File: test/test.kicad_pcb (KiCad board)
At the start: 2 copper layers, 100 x 100 mm, 107 parts, among them J1 UEXT_Host, J2 Conn_01x02, J3 Conn_02x06_Odd_Even, J4 Conn_02x06_Odd_Even, J5 Conn_02x06_Odd_Even, Q1 BC859, Q10 BC848, Q11 BC808, Q12 BC848, Q13 BC848, Q14 BC808, Q15 BC848, Q16 BC808, Q17 BC808, Q2 BC859, Q3 BC859, Q4 BC859, Q5 BC859, Q6 BC848, Q7 BC808, Q8 BC848, Q9 BC808, U3 PCA9531PW, U4 PCF8574AT, U6 TLC59108FPW

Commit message: work on 2nd update test
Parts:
- removed C1, C5, C6: C, PCM_Diode_SMD_Handsoldering_AKL:D_0603_1608Metric
- removed C2, C3, C4: C_Polarized, Capacitor_THT:CP_Radial_D5.0mm_P2.00mm
- removed D10, D11, D12, D13, D14, D15, D6, D7, D8, D9: LED, LED_THT:LED_D3.0mm
- removed J3, J4, J5: Conn_02x06_Odd_Even, Connector_PinHeader_2.54mm:PinHeader_2x06_P2.54mm_Vertical
- removed Q1, Q2, Q3, Q4, Q5: BC859, Package_TO_SOT_SMD:SOT-23
- removed Q10, Q12, Q13, Q15, Q6, Q8: BC848, Package_TO_SOT_SMD:SOT-23
- removed Q11, Q14, Q16, Q17, Q7, Q9: BC808, Package_TO_SOT_SMD:SOT-23
- removed R1, R10, R11, R12, R13, R14, R15, R16, R17, R18, R19, R2, R20, R3, R4, R5, R6, R7, R8, R9: R, Resistor_THT:R_Axial_DIN0204_L3.6mm_D1.6mm_P2.54mm_Vertical
- removed R21, R22, R23, R24, R25, R26, R27, R28, R29, R30, R31, R32, R33, R34, R35, R36, R37, R38, R39, R40, R41, R42, R43, R44, R45, R47, R48, R50, R51, R52, R53: 100k, Resistor_THT:R_Axial_DIN0204_L3.6mm_D1.6mm_P2.54mm_Vertical
- removed R46, R49: 1k, Resistor_THT:R_Axial_DIN0204_L3.6mm_D1.6mm_P2.54mm_Vertical
- removed U1: ~, petkn:THB Miniature Thumbstick THB001P
- added C10: 100n, Capacitor_SMD:C_0805_2012Metric_Pad1.18x1.45mm_HandSolder, B.Cu at (62.9, 127.3)
- added C11: 100n, Capacitor_SMD:C_0805_2012Metric_Pad1.18x1.45mm_HandSolder, B.Cu at (51.5, 127.2)
- added C12: 100n, Capacitor_SMD:C_0805_2012Metric_Pad1.18x1.45mm_HandSolder, B.Cu at (40.8, 126.8)
- added C13: 100n, Capacitor_SMD:C_0805_2012Metric_Pad1.18x1.45mm_HandSolder, B.Cu at (106.3, 124.4)
- added C14: 100n, Capacitor_SMD:C_0805_2012Metric_Pad1.18x1.45mm_HandSolder, B.Cu at (72.4, 135.0)
- added C15: 100u, Capacitor_SMD:C_1206_3216Metric_Pad1.33x1.80mm_HandSolder, B.Cu at (91.6, 134.7)
- added C16: 100u, Capacitor_SMD:C_1206_3216Metric_Pad1.33x1.80mm_HandSolder, B.Cu at (33.6, 134.1)
- added C17: 100n, Capacitor_SMD:C_0805_2012Metric_Pad1.18x1.45mm_HandSolder, B.Cu at (53.4, 134.9)
- added C18: 100u, Capacitor_SMD:C_1206_3216Metric_Pad1.33x1.80mm_HandSolder, B.Cu at (33.6, 105.5)
- added C7: 100n, Capacitor_SMD:C_0805_2012Metric_Pad1.18x1.45mm_HandSolder, B.Cu at (93.5, 124.4)
- added C8: 100n, Capacitor_SMD:C_0805_2012Metric_Pad1.18x1.45mm_HandSolder, B.Cu at (93.5, 121.4)
- added C9: 100n, Capacitor_SMD:C_0805_2012Metric_Pad1.18x1.45mm_HandSolder, B.Cu at (79.1, 127.5)
- added J6: New_PET_keyboard_connector, petkn:PET_New_Keyboard_Connector, F.Cu at (25.1, 100.8)
- added U7: 74LS145, Package_SO:SO-16_3.9x9.9mm_P1.27mm, B.Cu at (79.3, 118.3)
- added U8: ATmega32A-A, Package_QFP:TQFP-44_10x10mm_P0.8mm, B.Cu at (96.9, 102.5)
- added Y1: ASE-xxxMHz, Oscillator:Oscillator_SMD_Abracon_ASE-4Pin_3.2x2.5mm, B.Cu at (106.7, 118.6)
- D1, D2, D3, D4, D5: value LED -> SK6812MINI; footprint LED_THT:LED_D3.0mm -> LED_SMD:LED_SK6812MINI_PLCC4_3.5x3.5mm_P1.75mm; moved to B.Cu
- J1: value UEXT_Host -> AVR-ISP-6; footprint Connector_IDC:IDC-Header_2x05_P2.54mm_Vertical -> Connector_IDC:IDC-Header_2x03_P2.54mm_Vertical
- J2: value Conn_01x02 -> AVR-ISP-6; footprint Connector_PinHeader_2.54mm:PinHeader_1x02_P2.54mm_Vertical -> Connector_IDC:IDC-Header_2x03_P2.54mm_Vertical
- SW1: footprint petkn:SW_Cherry_MX_1.00u_PCB_with_LED -> CherryMX_PCB_LTST-A683CEGBW-Rotated:CherryMX_1.00u_PCB_LTST-A683CEGBW-Rotated
- SW2: value ~ -> CherryMX_LTST-A683CEGBW; footprint petkn:SW_Cherry_MX_1.00u_PCB_with_LED -> petkn:SW_Cherry_MX_1.00u_PCB_with_RGB_LED
- SW3, SW4, SW5: footprint petkn:SW_Cherry_MX_1.00u_PCB_with_LED -> petkn:SW_Cherry_MX_1.00u_PCB_with_RGB_LED
- U2: value ~ -> ATmega32A-A; footprint petkn:true-components-98002c3-ps2-ps3 -> Package_QFP:TQFP-44_10x10mm_P0.8mm; moved to B.Cu
- U3: value PCA9531PW -> 74HCT85; footprint Package_SO:TSSOP-16_4.4x5mm_P0.65mm -> Package_SO:SO-16_3.9x9.9mm_P1.27mm; moved to B.Cu
- U4: value PCF8574AT -> 74LS174; footprint Package_SO:SOIC-16W_7.5x10.3mm_P1.27mm -> Package_SO:SO-16_3.9x9.9mm_P1.27mm; moved to B.Cu
- U6: value TLC59108FPW -> 74LS174; footprint Package_SO:TSSOP-20_4.4x6.5mm_P0.65mm -> Package_SO:SO-16_3.9x9.9mm_P1.27mm; moved to B.Cu
- moved D2 79.1 mm to (24.7, 134.4)
- moved D1 74.4 mm to (44.1, 134.6)
- moved J2 71.1 mm to (95.2, 88.9)
- moved D3 58.0 mm to (63.5, 134.7)
- moved D5 54.2 mm to (101.7, 134.8)
- moved D4 52.8 mm to (82.7, 135.0)
- moved U6 51.6 mm to (40.6, 117.7)
- moved U3 46.9 mm to (63.2, 118.0)
- moved U4 29.9 mm to (51.4, 117.8)
- moved SW3 27.0 mm to (22.9, 153.3)
- moved J1 26.5 mm to (44.1, 87.7), turned to 90 degrees
- moved U5 19.2 mm to (72.1, 96.8)
- moved SW2 19.0 mm to (42.0, 153.3)
- moved U2 9.94 mm to (47.9, 101.4), turned to -90 degrees
- moved SW1 5.69 mm to (101.7, 148.2)
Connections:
- D1 pad 1: Net-(D1-K) -> Net-(D1-DOUT)
- D1 pad 2: Net-(D1-A) -> GND
- D2 pad 1: Net-(D12-K) -> Net-(D1-DIN)
- D2 pad 2: Net-(D2-A) -> GND
- D3 pad 1: Net-(D13-K) -> Net-(D3-DOUT)
- D3 pad 2: Net-(D3-A) -> GND
- D4 pad 1: Net-(D14-K) -> Net-(D4-DOUT)
- D4 pad 2: Net-(D4-A) -> GND
- D5 pad 1: Net-(D10-K) -> unconnected-(D5-DOUT-Pad1)
- D5 pad 2: Net-(D5-A) -> GND
- J1 pad 1: VCC -> Net-(J1-MISO)
- J1 pad 2: GND -> VCC
- J1 pad 3: unconnected-(J1-TXD-Pad3) -> Net-(J1-SCK)
- J1 pad 4: unconnected-(J1-RXD-Pad4) -> Net-(J1-MOSI)
- J1 pad 5: SCL -> Net-(J1-~{RST})
- J1 pad 6: SDA -> GND
- J2 pad 1: VCC5 -> Net-(J2-MISO)
- J2 pad 2: GND -> VCC
- SW1 pad 1: /RES -> Col1
- SW1 pad 2: GND -> Row0
- SW1 pad 3: Net-(D1-K) -> GND
- SW1 pad 4: Net-(R16-Pad1) -> Net-(SW1B-DIN)
- SW2 pad 3: Net-(D12-K) -> GND
- SW2 pad 4: Net-(R17-Pad1) -> Net-(SW1B-DOUT)
- SW3 pad 1: unconnected-(SW3-Pad1) -> Col5
- SW3 pad 2: unconnected-(SW3-Pad2) -> Row0
- SW3 pad 3: Net-(D13-K) -> GND
- SW4 pad 1: unconnected-(SW4-Pad1) -> Col5
- SW4 pad 2: unconnected-(SW4-Pad2) -> Row8
- SW4 pad 3: Net-(D14-K) -> GND
- SW4 pad 4: Net-(R19-Pad1) -> Net-(SW3B-DOUT)
- SW5 pad 1: unconnected-(SW5-Pad1) -> Col1
- SW5 pad 2: unconnected-(SW5-Pad2) -> Row8
- SW5 pad 3: Net-(D10-K) -> GND
- SW5 pad 4: Net-(R20-Pad1) -> Net-(SW4B-DOUT)
- U2 pad 1: (no net) -> Net-(J1-MOSI)
- U2 pad 10: Net-(J4-Pin_3) -> Net-(U2-PD1)
- U2 pad 11: Net-(J4-Pin_5) -> Net-(U2-PD2)
- U2 pad 12: Net-(J4-Pin_2) -> Net-(U2-PB4)
- U2 pad 13: Net-(J4-Pin_4) -> Col4
- U2 pad 14: Net-(J4-Pin_6) -> Col5
- U2 pad 2: (no net) -> Net-(J1-MISO)
- U2 pad 3: (no net) -> Net-(J1-SCK)
- U2 pad 4: (no net) -> Net-(J1-~{RST})
- U2 pad 5: Net-(J4-Pin_9) -> VCC
- U2 pad 6: Net-(J4-Pin_7) -> GND
- U2 pad 7: Net-(J4-Pin_10) -> unconnected-(U2-XTAL2-Pad7)
- U2 pad 8: Net-(J4-Pin_8) -> CLK16M
- U2 pad 9: Net-(J4-Pin_1) -> Net-(U2-PD0)
- U3 pad 1: GND -> S3
- U3 pad 10: unconnected-(U3-LED5-Pad10) -> Net-(U3-A0)
- U3 pad 11: unconnected-(U3-LED6-Pad11) -> S1
- U3 pad 12: unconnected-(U3-LED7-Pad12) -> Net-(U3-A1)
- U3 pad 13: /RES -> Net-(U3-A2)
- U3 pad 14: SCL -> S2
- U3 pad 15: SDA -> Net-(U3-A3)
- U3 pad 2: GND -> unconnected-(U3-Ia<b-Pad2)
- U3 pad 3: GND -> VCC
- U3 pad 4: PWM0 -> unconnected-(U3-Ia>b-Pad4)
- U3 pad 5: PWM1 -> unconnected-(U3-Oa>b-Pad5)
- U3 pad 6: PWM2 -> Net-(U2-PD2)
- U3 pad 7: PWM3 -> unconnected-(U3-Oa<b-Pad7)
- U3 pad 9: PWM4 -> S0
- U4 pad 1: GND -> VCC
- U4 pad 10: unconnected-(U4-P5-Pad10) -> Net-(U3-A2)
- U4 pad 11: unconnected-(U4-P6-Pad11) -> Net-(U4-D3)
- U4 pad 12: unconnected-(U4-P7-Pad12) -> Net-(U3-A1)
- U4 pad 13: unconnected-(U4-~{INT}-Pad13) -> Net-(U4-D4)
- U4 pad 14: SCL -> Net-(U4-D5)
- U4 pad 15: SDA -> Net-(U3-A0)
- U4 pad 2: GND -> Net-(U4-D3)
- U4 pad 3: GND -> Net-(U4-D0)
- U4 pad 4: ON0 -> Net-(U4-D1)
- U4 pad 5: ON1 -> Net-(U4-D2)
- U4 pad 6: ON2 -> Net-(U4-D2)
- U4 pad 7: ON3 -> Net-(U3-A3)
- U4 pad 9: unconnected-(U4-P4-Pad9) -> CLK16M
- U5 pad 10: Net-(J4-Pin_4) -> Col2
- U5 pad 11: Net-(J4-Pin_6) -> Row5
- U5 pad 12: Net-(J4-Pin_1) -> Row3
- U5 pad 13: Net-(J4-Pin_3) -> Col2
- U5 pad 14: Net-(J4-Pin_3) -> Row4
- U5 pad 5: Net-(J4-Pin_9) -> unconnected-(U5C-SW1_A-Pad5)
- U5 pad 6: Net-(J4-Pin_7) -> unconnected-(U5C-SW1_B-Pad6)
- U5 pad 7: Net-(J4-Pin_10) -> Col4
- U5 pad 8: Net-(J4-Pin_8) -> Row1
- U5 pad 9: Net-(J4-Pin_2) -> Row7
- U6 pad 1: unconnected-(U6-REXT-Pad1) -> VCC
- U6 pad 10: PWM3 -> Net-(U4-D1)
- U6 pad 11: PWM4 -> S3
- U6 pad 12: IO5 -> Net-(U4-D4)
- U6 pad 13: GND -> Net-(U6-D4)
- U6 pad 14: IO6 -> Net-(U6-D5)
- U6 pad 15: IO7 -> Net-(U4-D5)
- U6 pad 16: GND -> VCC
- U6 pad 2: GND -> Net-(U6-D5)
- U6 pad 3: GND -> S0
- U6 pad 4: GND -> S1
- U6 pad 5: GND -> Net-(U6-D4)
- U6 pad 6: PWM0 -> S2
- U6 pad 7: PWM1 -> Net-(U4-D0)
- U6 pad 9: PWM2 -> CLK16M
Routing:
- net VCC: track 262.3 -> 0.00 mm, vias 1 -> 0
- net /RES: track 190.4 -> 0.00 mm, vias 3 -> 0
- net Net-(D12-K): track 134.9 -> 0.00 mm, vias 1 -> 0
- net Net-(D1-K): track 118.3 -> 0.00 mm
- net VCC5: track 116.2 -> 0.00 mm
- net Net-(D14-K): track 104.2 -> 0.00 mm
- net Net-(D13-K): track 100.8 -> 0.00 mm, vias 1 -> 0
- net Net-(Q11-C): track 96.7 -> 0.00 mm
- net Net-(D10-K): track 96.2 -> 0.00 mm
- net Net-(R20-Pad1): track 83.2 -> 0.00 mm, vias 1 -> 0
- net Net-(J3-Pin_4): track 79.8 -> 0.00 mm
- net Net-(J3-Pin_3): track 78.6 -> 0.00 mm
- net Net-(J3-Pin_5): track 77.6 -> 0.00 mm
- net Net-(R16-Pad1): track 77.0 -> 0.00 mm, vias 2 -> 0
- net Net-(J3-Pin_2): track 74.4 -> 0.00 mm, vias 2 -> 0
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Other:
- board size 100 x 100 mm -> 100 x 81.9 mm

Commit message: work on 2nd update test
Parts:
- removed D1, D2, D3, D4, D5: SK6812MINI, LED_SMD:LED_SK6812MINI_PLCC4_3.5x3.5mm_P1.75mm
- added SW10: CherryMX_LTST-A683CEGBW, petkn:SW_Cherry_MX_1.00u_PCB_with_RGB_LED, F.Cu at (99.2, 134.2)
- added SW6: ~, petkn:SW_Cherry_MX_1.00u_PCB_with_RGB_LED, F.Cu at (22.9, 134.2)
- added SW7: ~, petkn:SW_Cherry_MX_1.00u_PCB_with_RGB_LED, F.Cu at (42.0, 134.2)
- added SW8: ~, petkn:SW_Cherry_MX_1.00u_PCB_with_RGB_LED, F.Cu at (61.0, 134.2)
- added SW9: ~, CherryMX_PCB_LTST-A683CEGBW-Rotated:CherryMX_1.00u_PCB_LTST-A683CEGBW-Rotated, F.Cu at (82.7, 129.1)
- moved C8 59.7 mm to (45.8, 85.5)
- moved SW2 57.2 mm to (99.1, 153.3)
- moved C13 45.4 mm to (84.8, 84.4)
- moved J2 33.4 mm to (63.5, 99.3)
- moved C7 32.7 mm to (102.7, 93.0), turned to 180 degrees
- moved U5 31.8 mm to (101.7, 108.4), turned to -90 degrees
- moved Y1 30.0 mm to (102.8, 88.8), turned to 180 degrees
- moved J1 19.4 mm to (63.5, 88.8)
- moved SW1 19.2 mm to (82.5, 148.2)
- moved SW5 19.2 mm to (60.9, 153.3)
- moved SW4 19.1 mm to (41.9, 153.3)
- moved U8 14.4 mm to (85.3, 94.0)
- moved C10 10.4 mm to (67.3, 117.9)
- moved C11 10.1 mm to (55.8, 118.0)
- moved C12 9.99 mm to (44.7, 117.6)
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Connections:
- C7 pad 1: unconnected-(C7-Pad1) -> V33
- C7 pad 2: unconnected-(C7-Pad2) -> GND
- SW2 pad 1: unconnected-(SW2-Pad1) -> Row0
- SW2 pad 2: unconnected-(SW2-Pad2) -> Col2
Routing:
- net VCC: track 0.00 -> 505.0 mm, vias 0 -> 25
- net GND: track 0.00 -> 451.1 mm, vias 0 -> 22
- net Col2: track 0.00 -> 163.2 mm, vias 0 -> 4
- net Net-(SW3B-DIN): track 0.00 -> 122.2 mm, vias 0 -> 4
- net Row0: track 0.00 -> 115.6 mm, vias 0 -> 1
- net SDA: track 0.00 -> 114.1 mm, vias 0 -> 4
- net Net-(SW6B-DIN): track 0.00 -> 114.1 mm, vias 0 -> 2
- net SCL: track 0.00 -> 111.0 mm, vias 0 -> 4
- net V33: track 0.00 -> 107.3 mm, vias 0 -> 1
- net Col3: track 0.00 -> 105.1 mm, vias 0 -> 3
- net Row4: track 0.00 -> 99.3 mm, vias 0 -> 4
- net Col5: track 0.00 -> 92.9 mm, vias 0 -> 1
- net CLK16M: track 0.00 -> 91.1 mm, vias 0 -> 5
- net Col1: track 0.00 -> 89.6 mm, vias 0 -> 1
- net S0: track 0.00 -> 79.7 mm, vias 0 -> 4
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
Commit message: production test pcb
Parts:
- added U1: LSF0204Q, Package_SO:TSSOP-14_4.4x5mm_P0.65mm, B.Cu at (36.1, 86.1)
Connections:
- J6 pad 28: SCL -> Net-(J6-SCL)
- J6 pad 29: SDA -> Net-(J6-SCA)
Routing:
- net GND: track 451.1 -> 515.3 mm, vias 22 -> 24
- net V33: track 107.3 -> 130.3 mm, vias 1 -> 3
- net SCL: track 111.0 -> 91.6 mm
- net SDA: track 114.1 -> 95.3 mm
- net Net-(J6-SCL): track 0.00 -> 14.0 mm
- net Net-(J6-SCA): track 0.00 -> 13.2 mm
- net VCC: track 505.0 -> 514.3 mm, vias 25 -> 26

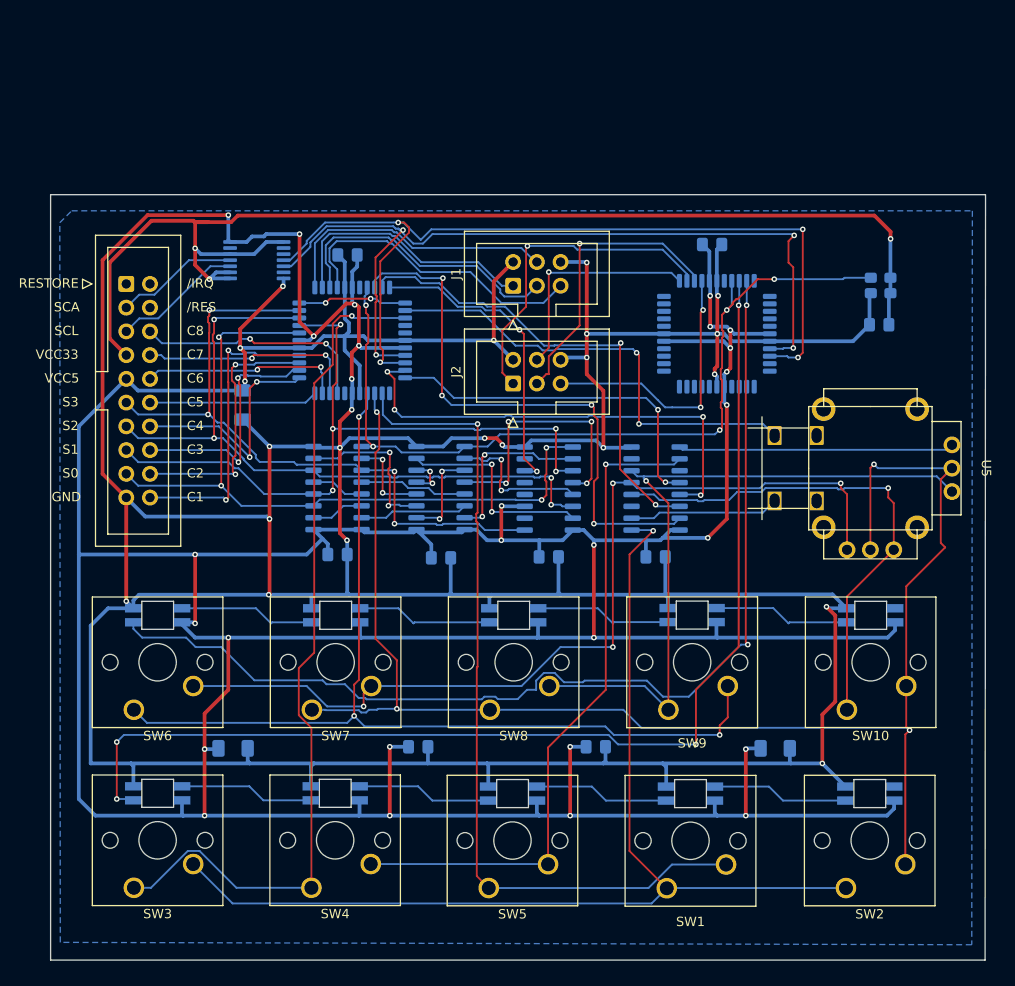
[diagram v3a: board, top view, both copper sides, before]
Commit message: add LSCS parts numbers
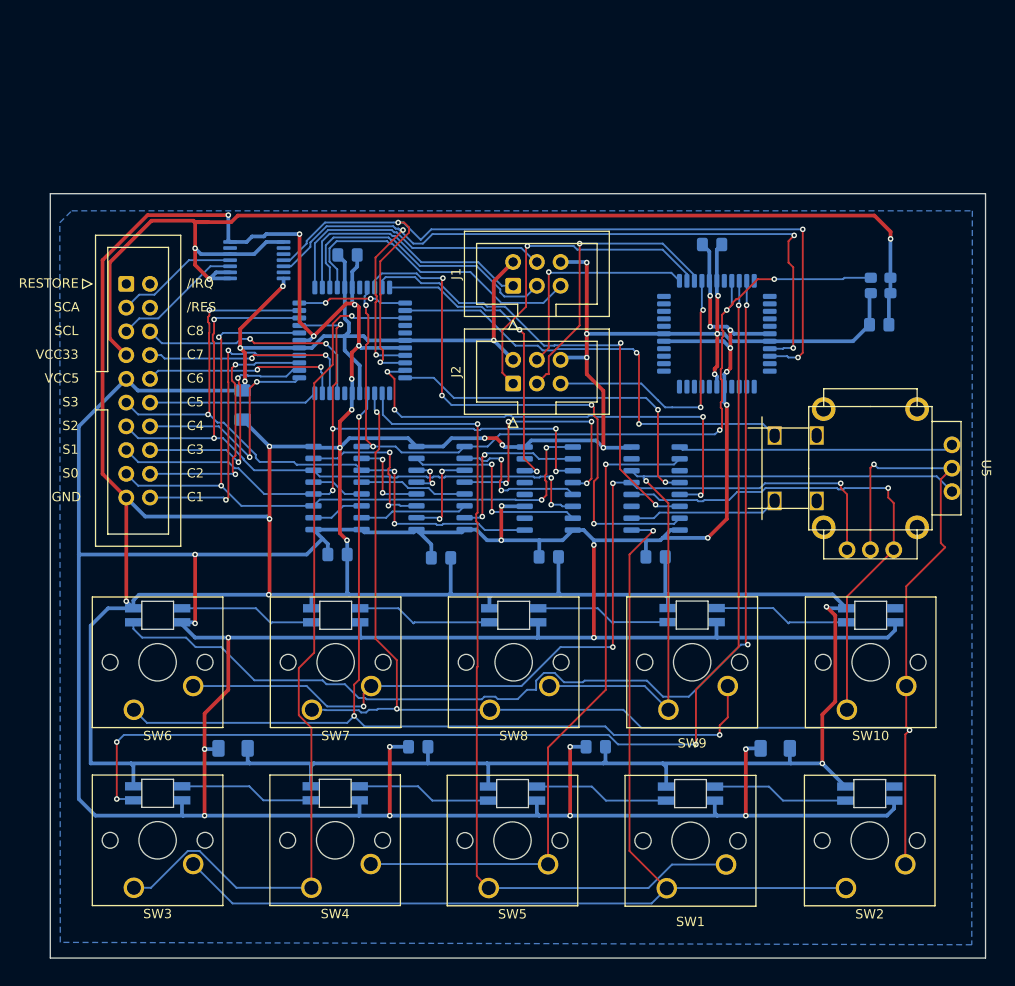
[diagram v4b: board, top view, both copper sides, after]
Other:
- board size 100 x 81.9 mm -> 100.1 x 81.8 mm
